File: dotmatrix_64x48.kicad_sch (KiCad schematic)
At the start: 67 parts, among them J1 Conn_01x03_Female, J2 Conn_01x03_Male, J3 Micro_SD_Card, J7 Conn_01x04_Female, P1 CONN_01X06, Q2 Q_NPN_BEC, Q4 Q_NPN_BEC, SW1 SW_PUSH_SMALL_H, SW2 SW_PUSH_SMALL_H, U1 74VHC541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

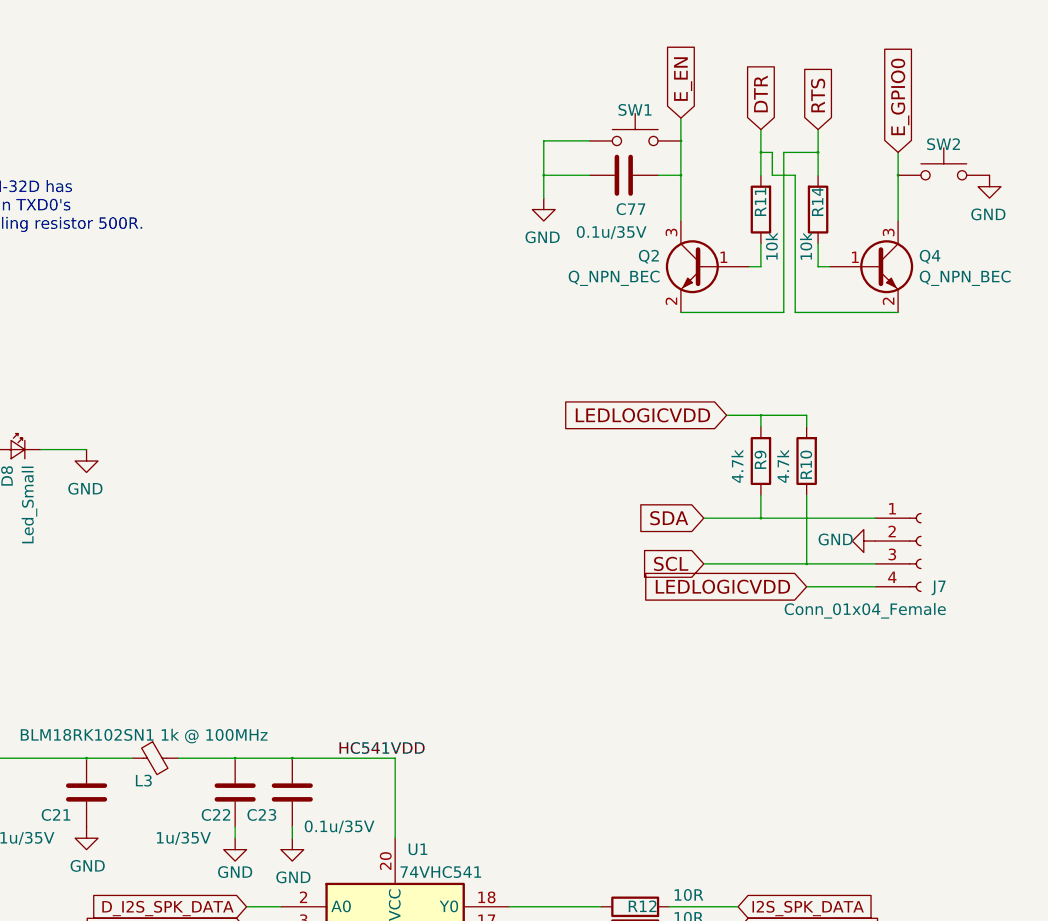
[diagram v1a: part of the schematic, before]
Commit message: Added an external pull-up resistor on GPIO0
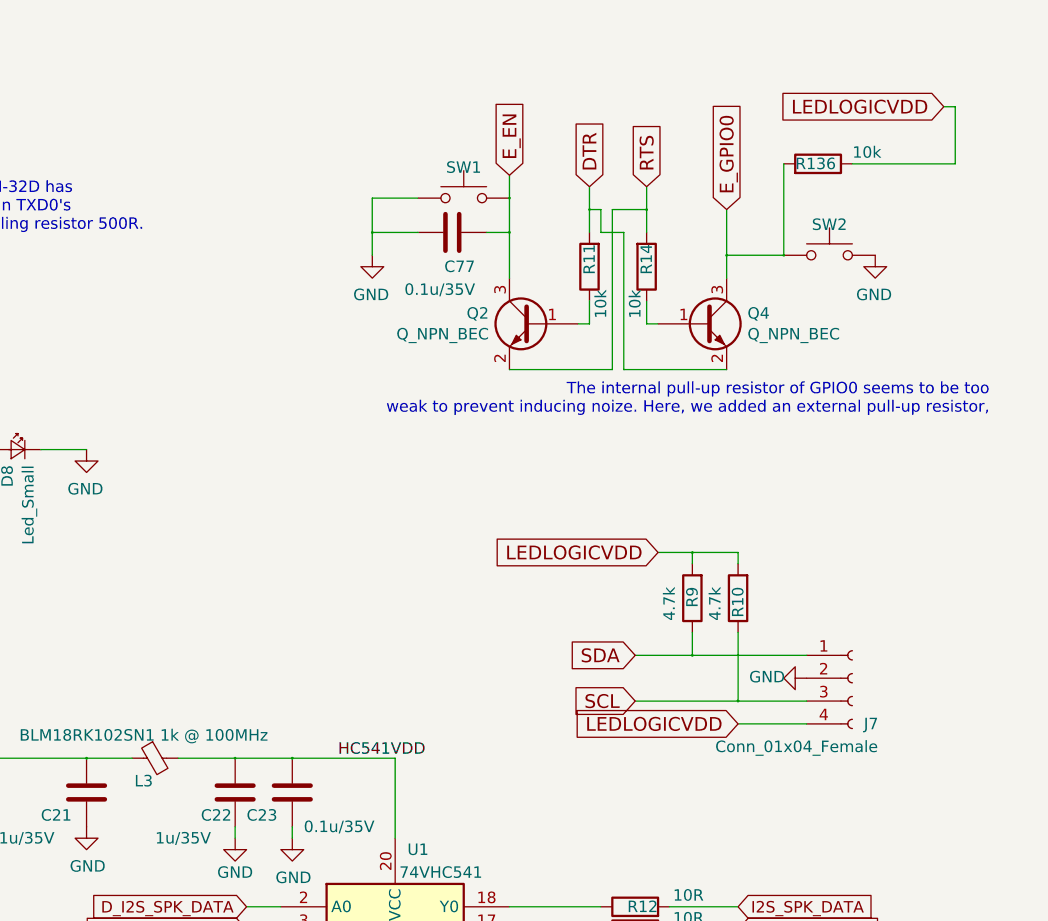
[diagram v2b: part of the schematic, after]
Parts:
- added R136: 10k, Resistor_SMD:R_0603_1608Metric_Pad1.05x0.95mm_HandSolder, symbol dotmatrix_64x48-rescue:R-device
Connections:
- net E_GPIO0: now also R136.2
- net LEDLOGICVDD: now also R136.1
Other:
- note added: "The internal pull-up resistor of GPIO0 seems to be too weak to prevent inducing noize. Here, we added an external pull-up resistor,"
- moved on the sheet: C77, J7, Q2, Q4, R10, R11, R14, R9, SW1, SW2

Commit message: Added some comments
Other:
- note added: "HC541 is required to drive relatively long lines. ESP8266 got unstable if it drives directly long line as this would. I'm not sure ESP32 has the same problem."
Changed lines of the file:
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@@
-(kicad_sch (version 20200820) (host eeschema "5.99.0-unknown-b0af66afc~103~ubuntu18.04.1")
+(kicad_sch (version 20200827) (generator eeschema)
   (page 1 10)
   (paper "A4")
@@
   (junction (at 254 83.82) (diameter 0.3048) (color 0 0 0 0))
   (junction (at 259.08 34.29) (diameter 0.3048) (color 0 0 0 0))
+  (no_connect (at 99.06 73.66))
+  (no_connect (at 101.6 73.66))
+  (no_connect (at 96.52 73.66))
+  (no_connect (at 48.26 87.63))
+  (no_connect (at 104.14 73.66))
   (no_connect (at 106.68 73.66))
-  (no_connect (at 48.26 87.63))
+  (no_connect (at 151.13 137.16))
+  (no_connect (at 125.73 27.94))
   (no_connect (at 109.22 73.66))
-  (no_connect (at 96.52 73.66))
-  (no_connect (at 99.06 73.66))
-  (no_connect (at 104.14 73.66))
-  (no_connect (at 125.73 27.94))
-  (no_connect (at 101.6 73.66))
-  (no_connect (at 151.13 137.16))
   (wire (pts (xy 20.32 92.71) (xy 39.37 92.71))
     (stroke (width 0) (type solid) (color 0 0 0 0))
@@
     (effects (font (size 1.27 1.27)) (justify right bottom))
   )
+  (text "HC541 is required to drive relatively long lines.\nESP8266 got unstable if it drives directly long line as this would.\nI'm not sure ESP32 has the same problem."
+    (at 257.81 152.4 0)
+    (effects (font (size 1.27 1.27)) (justify right bottom))
+  )

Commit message: Fixed some comments; Added FB on SCL/SDA line
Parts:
- added L? (x2): BLM18RK102SN1 1k @ 100MHz, Resistors_SMD:R_0603_HandSoldering, symbol dotmatrix_64x48-rescue:Ferrite_Bead_Small-device
- R74: value 120R -> 10R
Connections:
- net SCL: now also L?.2; no longer R75.1
- net SDA: now also L?.2; no longer R74.1
- new net: L?.1, R75.1
- new net: L?.1, R74.1
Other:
- note added: "HC541 is required to drive relatively long lines. ESP8266 got unstable if it drove directly long line as this would. I'm not sure ESP32 has the same problem."
- note removed: "HC541 is required to drive relatively long lines. ESP8266 got unstable if it drives directly long line as this would. I'm not sure ESP32 has the same problem."
- moved on the sheet: R75
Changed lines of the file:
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@@
   (junction (at 254 83.82) (diameter 0.3048) (color 0 0 0 0))
   (junction (at 259.08 34.29) (diameter 0.3048) (color 0 0 0 0))
+  (no_connect (at 109.22 73.66))
   (no_connect (at 99.06 73.66))
-  (no_connect (at 101.6 73.66))
+  (no_connect (at 125.73 27.94))
+  (no_connect (at 104.14 73.66))
   (no_connect (at 96.52 73.66))
   (no_connect (at 48.26 87.63))
-  (no_connect (at 104.14 73.66))
   (no_connect (at 106.68 73.66))
   (no_connect (at 151.13 137.16))
-  (no_connect (at 125.73 27.94))
-  (no_connect (at 109.22 73.66))
+  (no_connect (at 101.6 73.66))
   (wire (pts (xy 20.32 92.71) (xy 39.37 92.71))
     (stroke (width 0) (type solid) (color 0 0 0 0))
@@
     (stroke (width 0) (type solid) (color 0 0 0 0))
   )
-  (wire (pts (xy 127 24.13) (xy 139.7 24.13))
+  (wire (pts (xy 127 24.13) (xy 128.27 24.13))
     (stroke (width 0) (type solid) (color 0 0 0 0))
   )
@@
     (stroke (width 0) (type solid) (color 0 0 0 0))
   )
-  (wire (pts (xy 140.97 38.1) (xy 147.32 38.1))
+  (wire (pts (xy 140.97 38.1) (xy 171.45 38.1))
     (stroke (width 0) (type solid) (color 0 0 0 0))
   )
@@
     (stroke (width 0) (type solid) (color 0 0 0 0))
   )
+  (wire (pts (xy 144.78 24.13) (xy 135.89 24.13))
+    (stroke (width 0) (type solid) (color 0 0 0 0))
+  )
   (wire (pts (xy 146.05 43.18) (xy 140.97 43.18))
     (stroke (width 0) (type solid) (color 0 0 0 0))
@@
     (stroke (width 0) (type solid) (color 0 0 0 0))
   )
-  (wire (pts (xy 153.67 24.13) (xy 147.32 24.13))
+  (wire (pts (xy 153.67 24.13) (xy 149.86 24.13))
     (stroke (width 0) (type solid) (color 0 0 0 0))
   )
@@
   )
   (wire (pts (xy 171.45 90.17) (xy 181.61 90.17))
+    (stroke (width 0) (type solid) (color 0 0 0 0))
+  )
+  (wire (pts (xy 176.53 38.1) (xy 185.42 38.1))
     (stroke (width 0) (type solid) (color 0 0 0 0))
   )
@@
     (effects (font (size 1.27 1.27)) (justify right bottom))
   )
-  (text "HC541 is required to drive relatively long lines.\nESP8266 got unstable if it drives directly long line as this would.\nI'm not sure ESP32 has the same problem."
-    (at 257.81 152.4 0)
-    (effects (font (size 1.27 1.27)) (justify right bottom))
+  (text "HC541 is required to drive relatively long lines.\nESP8266 got unstable if it drove directly long line as this would.\nI'm not sure ESP32 has the same problem."
+    (at 199.39 153.67 0)
+    (effects (font (size 1.27 1.27)) (justify left bottom))
   )
   (text "The internal pull-up resistor of GPIO0 seems to be too\nweak to prevent inducing noize. Here, we added an external pull-up resistor,"
@@
     (effects (font (size 1.524 1.524)) (justify left))
   )
-  (global_label "SDA" (shape input) (at 147.32 38.1 0)
-    (effects (font (size 1.524 1.524)) (justify left))
-  )
   (global_label "E_TX2" (shape input) (at 147.32 50.8 0)
     (effects (font (size 1.27 1.27)) (justify left))
@@
   (global_label "LED1642VDD" (shape input) (at 171.45 90.17 180)
     (effects (font (size 1.524 1.524)) (justify right))
+  )
+  (global_label "SDA" (shape input) (at 185.42 38.1 0)
+    (effects (font (size 1.524 1.524)) (justify left))
   )
   (global_label "D_I2S_SPK_DATA" (shape input) (at 199.39 106.68 180)
@@
     (property "Datasheet" "" (id 3) (at 115.57 160.02 0))
   )
+  (symbol (lib_id "dotmatrix_64x48-rescue:R-device") (at 132.08 24.13 270) (mirror x) (unit 1)
+    (in_bom yes) (on_board yes)
+    (property "Reference" "R75" (id 0) (at 129.54 24.13 90)
+      (effects (font (size 1.27 1.27)) (justify left))
+    )
+    (property "Value" "10R" (id 1) (at 135.89 25.4 90)
+      (effects (font (size 1.27 1.27)) (justify left))
+    )
+    (property "Footprint" "Resistor_SMD:R_0603_1608Metric_Pad1.05x0.95mm_HandSolder" (id 2) (at 132.08 25.908 90)
+      (effects (font (size 1.27 1.27)) hide)
+    )
+    (property "Datasheet" "" (id 3) (at 132.08 24.13 0))
+  )
   (symbol (lib_id "dotmatrix_64x48-rescue:R-device") (at 137.16 33.02 270) (mirror x) (unit 1)
     (in_bom yes) (on_board yes)
@@
       (effects (font (size 1.27 1.27)) (justify left))
     )
-    (property "Value" "120R" (id 1) (at 129.54 36.83 90)
+    (property "Value" "10R" (id 1) (at 129.54 36.83 90)
       (effects (font (size 1.27 1.27)) (justify left))
     )
@@
     )
     (property "Datasheet" "" (id 3) (at 137.16 58.42 0))
-  )
-  (symbol (lib_id "dotmatrix_64x48-rescue:R-device") (at 143.51 24.13 270) (mirror x) (unit 1)
-    (in_bom yes) (on_board yes)
-    (property "Reference" "R75" (id 0) (at 140.97 24.13 90)
-      (effects (font (size 1.27 1.27)) (justify left))
-    )
-    (property "Value" "10R" (id 1) (at 147.32 25.4 90)
-      (effects (font (size 1.27 1.27)) (justify left))
-    )
-    (property "Footprint" "Resistor_SMD:R_0603_1608Metric_Pad1.05x0.95mm_HandSolder" (id 2) (at 143.51 25.908 90)
-      (effects (font (size 1.27 1.27)) hide)
-    )
-    (property "Datasheet" "" (id 3) (at 143.51 24.13 0))
   )
   (symbol (lib_id "dotmatrix_64x48-rescue:R-device") (at 237.49 35.56 180) (unit 1)
@@
     )
     (property "Datasheet" "" (id 3) (at 100.33 173.99 0))
+  )
+  (symbol (lib_id "dotmatrix_64x48-rescue:Ferrite_Bead_Small-device") (at 147.32 24.13 90) (mirror x) (unit 1)
+    (in_bom yes) (on_board yes)
+    (property "Reference" "L?" (id 0) (at 146.05 26.67 90))
+    (property "Value" "BLM18RK102SN1 1k @ 100MHz" (id 1) (at 146.05 21.59 90))
+    (property "Footprint" "Resistors_SMD:R_0603_HandSoldering" (id 2) (at 147.32 24.13 0)
+      (effects (font (size 1.27 1.27)) hide)
+    )
+    (property "Datasheet" "" (id 3) (at 147.32 24.13 0))
+  )
+  (symbol (lib_id "dotmatrix_64x48-rescue:Ferrite_Bead_Small-device") (at 173.99 38.1 90) (mirror x) (unit 1)
+    (in_bom yes) (on_board yes)
+    (property "Reference" "L?" (id 0) (at 172.72 40.64 90))
+    (property "Value" "BLM18RK102SN1 1k @ 100MHz" (id 1) (at 172.72 35.56 90))
+    (property "Footprint" "Resistors_SMD:R_0603_HandSoldering" (id 2) (at 173.99 38.1 0)
+      (effects (font (size 1.27 1.27)) hide)
+    )
+    (property "Datasheet" "" (id 3) (at 173.99 38.1 0))
   )
   (symbol (lib_id "dotmatrix_64x48-rescue:Ferrite_Bead_Small-device") (at 189.23 90.17 90) (mirror x) (unit 1)
@@
       (reference "L5") (unit 1)
     )
+    (path "/9e0326f7-50f2-4702-8dfc-880eee015938"
+      (reference "L?") (unit 1)
+    )
+    (path "/c788adc5-bd1b-4179-9658-5ebe5800a5bd"
+      (reference "L?") (unit 1)
+    )
     (path "/00000000-0000-0000-0000-00005bb4df6a"
       (reference "P1") (unit 1)
@@
       (reference "#PWR0164") (unit 1)
     )
+    (path "/00000000-0000-0000-0000-000057bb11db/45a0d4ff-a4aa-4e12-90f3-7d7fc9d24a76"
+      (reference "#PWR?") (unit 1)
+    )
+    (path "/00000000-0000-0000-0000-000057bb11db/6e021b66-8bb4-43ec-a0cd-2d4260eda0fd"
+      (reference "#PWR?") (unit 1)
+    )
+    (path "/00000000-0000-0000-0000-000057bb11db/7f9ae4e6-3b9c-4d57-a50a-3970e41497b9"
+      (reference "#PWR?") (unit 1)
+    )
     (path "/00000000-0000-0000-0000-000057bb11db/00000000-0000-0000-0000-00005bbd3352"
